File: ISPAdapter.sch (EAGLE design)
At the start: 3 parts

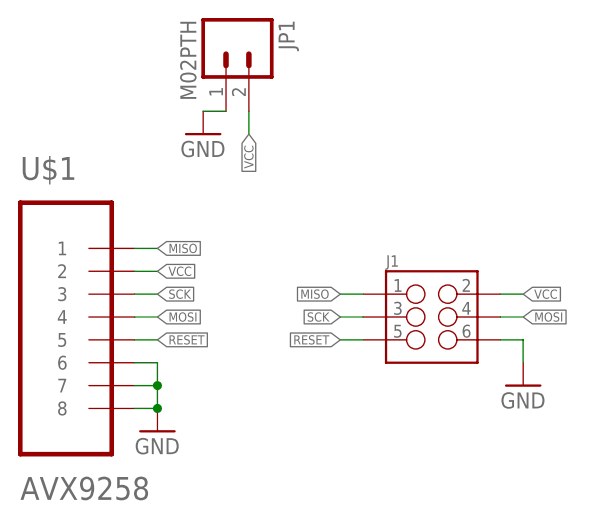
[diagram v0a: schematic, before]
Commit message: Dropped ground layer
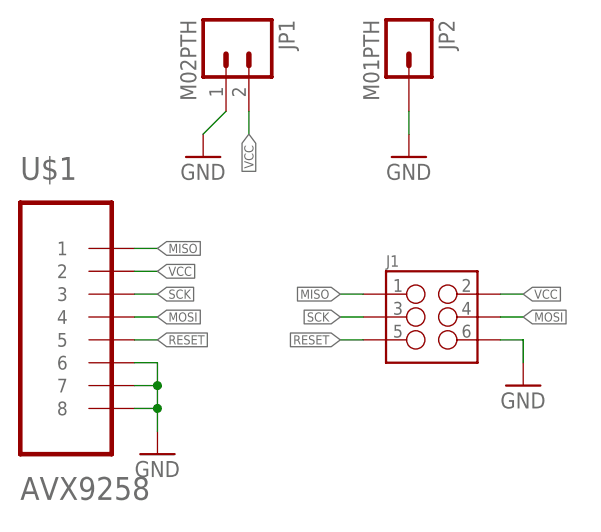
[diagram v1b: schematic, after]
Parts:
- added JP2: M01PTH, SparkFun-Connectors:M01PTH
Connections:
- net GND: now also JP2.1
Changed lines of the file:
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@@
 <part name="U$1" library="dubec" deviceset="AVX9258" device=""/>
 <part name="GND4" library="SparkFun-Aesthetics" deviceset="GND" device=""/>
+<part name="JP2" library="SparkFun-Connectors" deviceset="M01" device="PTH"/>
+<part name="GND1" library="SparkFun-Aesthetics" deviceset="GND" device=""/>
 </parts>
 <sheets>
@@
 <instance part="J1" gate="G$1" x="81.28" y="60.96"/>
 <instance part="JP1" gate="G$1" x="58.42" y="91.44" rot="R270"/>
-<instance part="GND3" gate="1" x="55.88" y="81.28"/>
+<instance part="GND3" gate="1" x="55.88" y="78.74"/>
 <instance part="U$1" gate="G$1" x="40.64" y="60.96"/>
-<instance part="GND4" gate="1" x="50.8" y="48.26"/>
+<instance part="GND4" gate="1" x="50.8" y="45.72"/>
+<instance part="JP2" gate="G$1" x="78.74" y="91.44" rot="R270"/>
+<instance part="GND1" gate="1" x="78.74" y="78.74"/>
 </instances>
 <busses>
@@
 <segment>
 <pinref part="JP1" gate="G$1" pin="1"/>
-<wire x1="58.42" y1="83.82" x2="55.88" y2="83.82" width="0.1524" layer="91"/>
+<wire x1="58.42" y1="83.82" x2="55.88" y2="81.28" width="0.1524" layer="91"/>
 <pinref part="GND3" gate="1" pin="GND"/>
 </segment>
 <segment>
 <pinref part="U$1" gate="G$1" pin="8"/>
-<wire x1="48.26" y1="50.8" x2="50.8" y2="50.8" width="0.1524" layer="91"/>
 <pinref part="GND4" gate="1" pin="GND"/>
 <pinref part="U$1" gate="G$1" pin="6"/>
@@
 <wire x1="50.8" y1="53.34" x2="50.8" y2="50.8" width="0.1524" layer="91"/>
 <junction x="50.8" y="53.34"/>
+<wire x1="50.8" y1="50.8" x2="50.8" y2="48.26" width="0.1524" layer="91"/>
+<wire x1="48.26" y1="50.8" x2="50.8" y2="50.8" width="0.1524" layer="91"/>
 <junction x="50.8" y="50.8"/>
 </segment>
+<segment>
+<pinref part="JP2" gate="G$1" pin="1"/>
+<pinref part="GND1" gate="1" pin="GND"/>
+<wire x1="78.74" y1="83.82" x2="78.74" y2="81.28" width="0.1524" layer="91"/>
+</segment>
 </net>

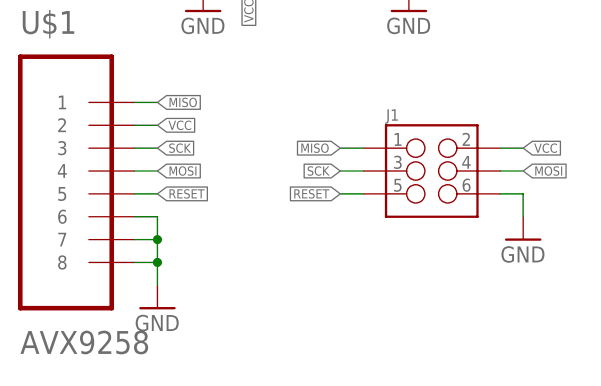
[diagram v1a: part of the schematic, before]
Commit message: Grounded screw holes; disconnected unused connector pins
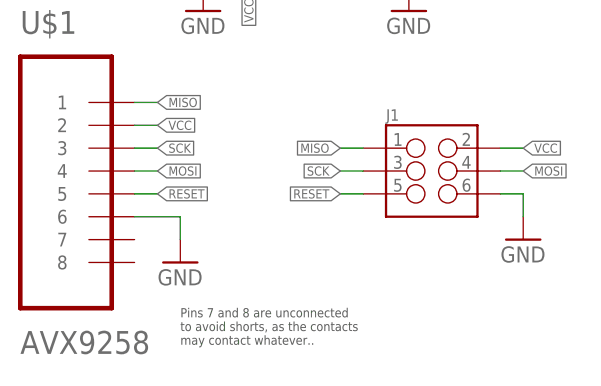
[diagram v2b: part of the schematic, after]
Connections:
- net GND: no longer U$1.7, U$1.8
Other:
- note added: "Pins 7 and 8 are unconnected to avoid shorts, as the contacts may contact whatever.."
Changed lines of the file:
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@@
 <sheet>
 <plain>
+<text x="53.34" y="45.72" size="1.016" layer="97" align="top-left">Pins 7 and 8 are unconnected
+to avoid shorts, as the contacts
+may contact whatever..</text>
 </plain>
 <instances>
@@
 <instance part="GND3" gate="1" x="55.88" y="78.74"/>
 <instance part="U$1" gate="G$1" x="40.64" y="60.96"/>
-<instance part="GND4" gate="1" x="50.8" y="45.72"/>
+<instance part="GND4" gate="1" x="53.34" y="50.8"/>
 <instance part="JP2" gate="G$1" x="78.74" y="91.44" rot="R270"/>
 <instance part="GND1" gate="1" x="78.74" y="78.74"/>
@@
 </segment>
 <segment>
-<pinref part="U$1" gate="G$1" pin="8"/>
-<pinref part="GND4" gate="1" pin="GND"/>
-<pinref part="U$1" gate="G$1" pin="6"/>
-<wire x1="48.26" y1="55.88" x2="50.8" y2="55.88" width="0.1524" layer="91"/>
-<pinref part="U$1" gate="G$1" pin="7"/>
-<wire x1="48.26" y1="53.34" x2="50.8" y2="53.34" width="0.1524" layer="91"/>
-<wire x1="50.8" y1="55.88" x2="50.8" y2="53.34" width="0.1524" layer="91"/>
-<wire x1="50.8" y1="53.34" x2="50.8" y2="50.8" width="0.1524" layer="91"/>
-<junction x="50.8" y="53.34"/>
-<wire x1="50.8" y1="50.8" x2="50.8" y2="48.26" width="0.1524" layer="91"/>
-<wire x1="48.26" y1="50.8" x2="50.8" y2="50.8" width="0.1524" layer="91"/>
-<junction x="50.8" y="50.8"/>
-</segment>
-<segment>
 <pinref part="JP2" gate="G$1" pin="1"/>
 <pinref part="GND1" gate="1" pin="GND"/>
 <wire x1="78.74" y1="83.82" x2="78.74" y2="81.28" width="0.1524" layer="91"/>
 </segment>
+<segment>
+<pinref part="U$1" gate="G$1" pin="6"/>
+<wire x1="48.26" y1="55.88" x2="53.34" y2="55.88" width="0.1524" layer="91"/>
+<pinref part="GND4" gate="1" pin="GND"/>
+<wire x1="53.34" y1="55.88" x2="53.34" y2="53.34" width="0.1524" layer="91"/>
+</segment>
 </net>

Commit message: Kelvin join?
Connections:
- new net DGND: J1.6, JP1.1, U$1.6
- net GND: no longer J1.6, JP1.1, U$1.6
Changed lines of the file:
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@@
 </segment>
 </net>
-<net name="GND" class="0">
+<net name="DGND" class="0">
 <segment>
 <pinref part="J1" gate="G$1" pin="6"/>
@@
 <wire x1="58.42" y1="83.82" x2="55.88" y2="81.28" width="0.1524" layer="91"/>
 <pinref part="GND3" gate="1" pin="GND"/>
-</segment>
-<segment>
-<pinref part="JP2" gate="G$1" pin="1"/>
-<pinref part="GND1" gate="1" pin="GND"/>
-<wire x1="78.74" y1="83.82" x2="78.74" y2="81.28" width="0.1524" layer="91"/>
 </segment>
 <segment>
@@
 </segment>
 </net>
+<net name="GND" class="0">
+<segment>
+<pinref part="JP2" gate="G$1" pin="1"/>
+<wire x1="78.74" y1="83.82" x2="78.74" y2="81.28" width="0.1524" layer="91"/>
+<pinref part="GND1" gate="1" pin="GND"/>
+</segment>
+</net>

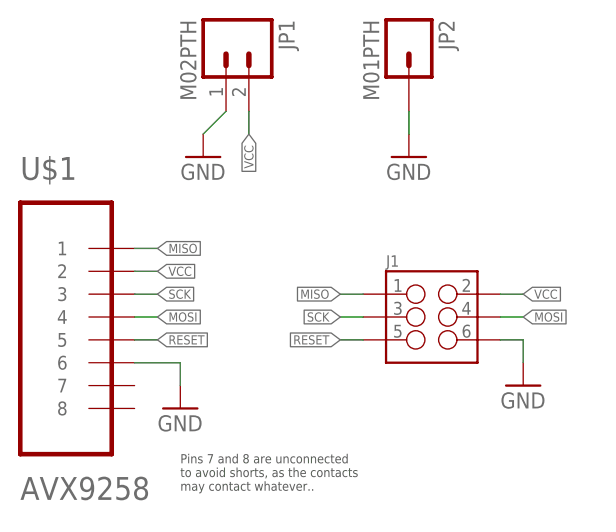
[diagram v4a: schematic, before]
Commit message: Adapter wiring to match DUBEC 1.5
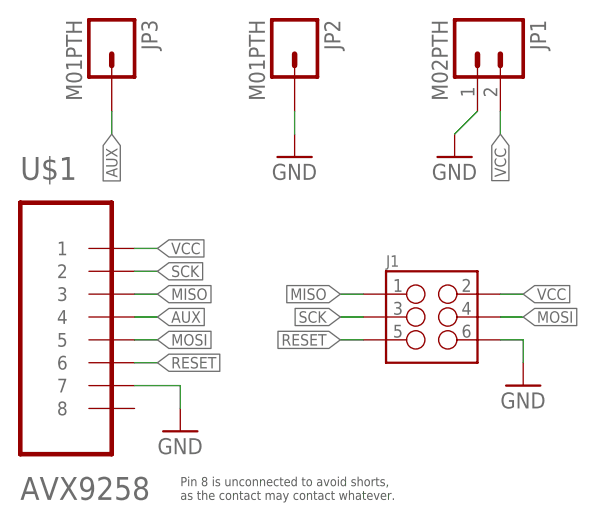
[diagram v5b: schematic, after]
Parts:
- added JP3: M01PTH, SparkFun-Connectors:M01PTH
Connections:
- new net AUX: JP3.1, U$1.4
- net DGND: now also U$1.7; no longer U$1.6
- net MISO: now also U$1.3; no longer U$1.1
- net MOSI: now also U$1.5; no longer U$1.4
- net RESET: now also U$1.6; no longer U$1.5
- net SCK: now also U$1.2; no longer U$1.3
- net VCC: now also U$1.1; no longer U$1.2
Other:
- note added: "Pin 8 is unconnected to avoid shorts, as the contact may contact whatever."
- note removed: "Pins 7 and 8 are unconnected to avoid shorts, as the contacts may contact whatever.."
- moved on the sheet: JP1, JP2
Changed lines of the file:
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@@
 <part name="JP2" library="SparkFun-Connectors" deviceset="M01" device="PTH"/>
 <part name="GND1" library="SparkFun-Aesthetics" deviceset="GND" device=""/>
+<part name="JP3" library="SparkFun-Connectors" deviceset="M01" device="PTH"/>
 </parts>
 <sheets>
 <sheet>
 <plain>
-<text x="53.34" y="45.72" size="1.016" layer="97" align="top-left">Pins 7 and 8 are unconnected
-to avoid shorts, as the contacts
-may contact whatever..</text>
+<text x="53.34" y="43.18" size="1.016" layer="97" align="top-left">Pin 8 is unconnected to avoid shorts,
+as the contact may contact whatever.</text>
 </plain>
 <instances>
 <instance part="GND2" gate="1" x="91.44" y="53.34"/>
 <instance part="J1" gate="G$1" x="81.28" y="60.96"/>
-<instance part="JP1" gate="G$1" x="58.42" y="91.44" rot="R270"/>
-<instance part="GND3" gate="1" x="55.88" y="78.74"/>
+<instance part="JP1" gate="G$1" x="86.36" y="91.44" rot="R270"/>
+<instance part="GND3" gate="1" x="83.82" y="78.74"/>
 <instance part="U$1" gate="G$1" x="40.64" y="60.96"/>
-<instance part="GND4" gate="1" x="53.34" y="50.8"/>
-<instance part="JP2" gate="G$1" x="78.74" y="91.44" rot="R270"/>
-<instance part="GND1" gate="1" x="78.74" y="78.74"/>
+<instance part="GND4" gate="1" x="53.34" y="48.26"/>
+<instance part="JP2" gate="G$1" x="66.04" y="91.44" rot="R270"/>
+<instance part="GND1" gate="1" x="66.04" y="78.74"/>
+<instance part="JP3" gate="G$1" x="45.72" y="91.44" rot="R270"/>
 </instances>
 <busses>
@@
 <pinref part="J1" gate="G$1" pin="2"/>
 <wire x1="88.9" y1="63.5" x2="91.44" y2="63.5" width="0.1524" layer="91"/>
-<label x="91.44" y="63.5" size="1.016" layer="95" xref="yes"/>
+<label x="91.44" y="63.5" size="1.27" layer="95" xref="yes"/>
 </segment>
 <segment>
 <pinref part="JP1" gate="G$1" pin="2"/>
-<wire x1="60.96" y1="83.82" x2="60.96" y2="81.28" width="0.1524" layer="91"/>
-<label x="60.96" y="81.28" size="1.016" layer="95" rot="R270" xref="yes"/>
+<wire x1="88.9" y1="83.82" x2="88.9" y2="81.28" width="0.1524" layer="91"/>
+<label x="88.9" y="81.28" size="1.27" layer="95" rot="R270" xref="yes"/>
 </segment>
 <segment>
-<pinref part="U$1" gate="G$1" pin="2"/>
-<wire x1="48.26" y1="66.04" x2="50.8" y2="66.04" width="0.1524" layer="91"/>
-<label x="50.8" y="66.04" size="1.016" layer="95" xref="yes"/>
+<pinref part="U$1" gate="G$1" pin="1"/>
+<wire x1="48.26" y1="68.58" x2="50.8" y2="68.58" width="0.1524" layer="91"/>
+<label x="50.8" y="68.58" size="1.27" layer="95" xref="yes"/>
 </segment>
 </net>
@@
 <pinref part="J1" gate="G$1" pin="4"/>
 <wire x1="88.9" y1="60.96" x2="91.44" y2="60.96" width="0.1524" layer="91"/>
-<label x="91.44" y="60.96" size="1.016" layer="95" xref="yes"/>
+<label x="91.44" y="60.96" size="1.27" layer="95" xref="yes"/>
 </segment>
 <segment>
-<pinref part="U$1" gate="G$1" pin="4"/>
-<wire x1="48.26" y1="60.96" x2="50.8" y2="60.96" width="0.1524" layer="91"/>
-<label x="50.8" y="60.96" size="1.016" layer="95" xref="yes"/>
+<pinref part="U$1" gate="G$1" pin="5"/>
+<wire x1="48.26" y1="58.42" x2="50.8" y2="58.42" width="0.1524" layer="91"/>
+<label x="50.8" y="58.42" size="1.27" layer="95" xref="yes"/>
 </segment>
 </net>
@@
 <segment>
 <pinref part="JP1" gate="G$1" pin="1"/>
-<wire x1="58.42" y1="83.82" x2="55.88" y2="81.28" width="0.1524" layer="91"/>
+<wire x1="86.36" y1="83.82" x2="83.82" y2="81.28" width="0.1524" layer="91"/>
 <pinref part="GND3" gate="1" pin="GND"/>
 </segment>
 <segment>
-<pinref part="U$1" gate="G$1" pin="6"/>
-<wire x1="48.26" y1="55.88" x2="53.34" y2="55.88" width="0.1524" layer="91"/>
 <pinref part="GND4" gate="1" pin="GND"/>
-<wire x1="53.34" y1="55.88" x2="53.34" y2="53.34" width="0.1524" layer="91"/>
+<wire x1="53.34" y1="53.34" x2="53.34" y2="50.8" width="0.1524" layer="91"/>
+<pinref part="U$1" gate="G$1" pin="7"/>
+<wire x1="53.34" y1="53.34" x2="48.26" y2="53.34" width="0.1524" layer="91"/>
 </segment>
 </net>
@@
 <pinref part="J1" gate="G$1" pin="1"/>
 <wire x1="73.66" y1="63.5" x2="71.12" y2="63.5" width="0.1524" layer="91"/>
-<label x="71.12" y="63.5" size="1.016" layer="95" rot="R180" xref="yes"/>
+<label x="71.12" y="63.5" size="1.27" layer="95" rot="R180" xref="yes"/>
 </segment>
 <segment>
-<pinref part="U$1" gate="G$1" pin="1"/>
-<wire x1="48.26" y1="68.58" x2="50.8" y2="68.58" width="0.1524" layer="91"/>
-<label x="50.8" y="68.58" size="1.016" layer="95" xref="yes"/>
+<pinref part="U$1" gate="G$1" pin="3"/>
+<wire x1="48.26" y1="63.5" x2="50.8" y2="63.5" width="0.1524" layer="91"/>
+<label x="50.8" y="63.5" size="1.27" layer="95" xref="yes"/>
 </segment>
 </net>
@@
 <pinref part="J1" gate="G$1" pin="3"/>
 <wire x1="73.66" y1="60.96" x2="71.12" y2="60.96" width="0.1524" layer="91"/>
-<label x="71.12" y="60.96" size="1.016" layer="95" rot="R180" xref="yes"/>
+<label x="71.12" y="60.96" size="1.27" layer="95" rot="R180" xref="yes"/>
 </segment>
 <segment>
-<pinref part="U$1" gate="G$1" pin="3"/>
-<wire x1="48.26" y1="63.5" x2="50.8" y2="63.5" width="0.1524" layer="91"/>
-<label x="50.8" y="63.5" size="1.016" layer="95" xref="yes"/>
+<pinref part="U$1" gate="G$1" pin="2"/>
+<wire x1="48.26" y1="66.04" x2="50.8" y2="66.04" width="0.1524" layer="91"/>
+<label x="50.8" y="66.04" size="1.27" layer="95" xref="yes"/>
 </segment>
 </net>
@@
 <pinref part="J1" gate="G$1" pin="5"/>
 <wire x1="73.66" y1="58.42" x2="71.12" y2="58.42" width="0.1524" layer="91"/>
-<label x="71.12" y="58.42" size="1.016" layer="95" rot="R180" xref="yes"/>
+<label x="71.12" y="58.42" size="1.27" layer="95" rot="R180" xref="yes"/>
 </segment>
 <segment>
-<pinref part="U$1" gate="G$1" pin="5"/>
-<wire x1="48.26" y1="58.42" x2="50.8" y2="58.42" width="0.1524" layer="91"/>
-<label x="50.8" y="58.42" size="1.016" layer="95" xref="yes"/>
+<pinref part="U$1" gate="G$1" pin="6"/>
+<wire x1="48.26" y1="55.88" x2="50.8" y2="55.88" width="0.1524" layer="91"/>
+<label x="50.8" y="55.88" size="1.27" layer="95" xref="yes"/>
 </segment>
 </net>
@@
 <segment>
 <pinref part="JP2" gate="G$1" pin="1"/>
-<wire x1="78.74" y1="83.82" x2="78.74" y2="81.28" width="0.1524" layer="91"/>
+<wire x1="66.04" y1="83.82" x2="66.04" y2="81.28" width="0.1524" layer="91"/>
 <pinref part="GND1" gate="1" pin="GND"/>
 </segment>
 </net>
+<net name="AUX" class="0">
+<segment>
+<pinref part="U$1" gate="G$1" pin="4"/>
+<wire x1="48.26" y1="60.96" x2="50.8" y2="60.96" width="0.1524" layer="91"/>
+<label x="50.8" y="60.96" size="1.27" layer="95" xref="yes"/>
+</segment>
+<segment>
+<pinref part="JP3" gate="G$1" pin="1"/>
+<wire x1="45.72" y1="83.82" x2="45.72" y2="81.28" width="0.1524" layer="91"/>
+<label x="45.72" y="81.28" size="1.27" layer="95" rot="R270" xref="yes"/>
+</segment>
+</net>

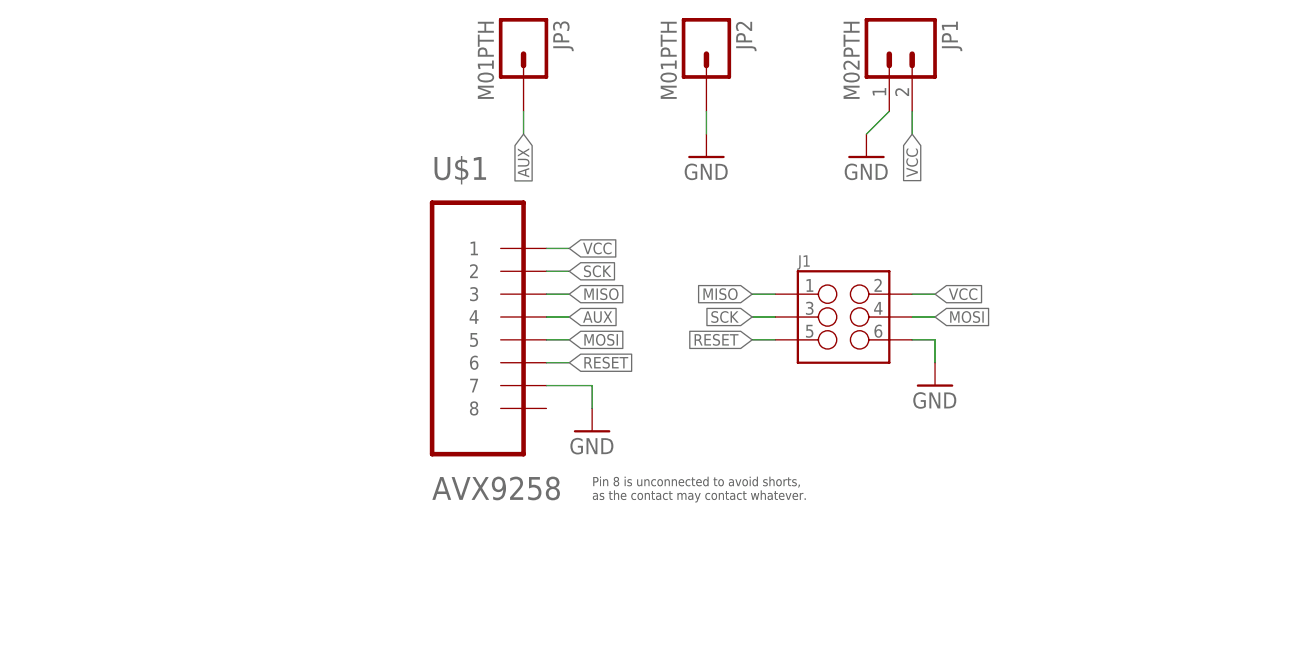
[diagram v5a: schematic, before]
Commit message: ISP/DW-switch
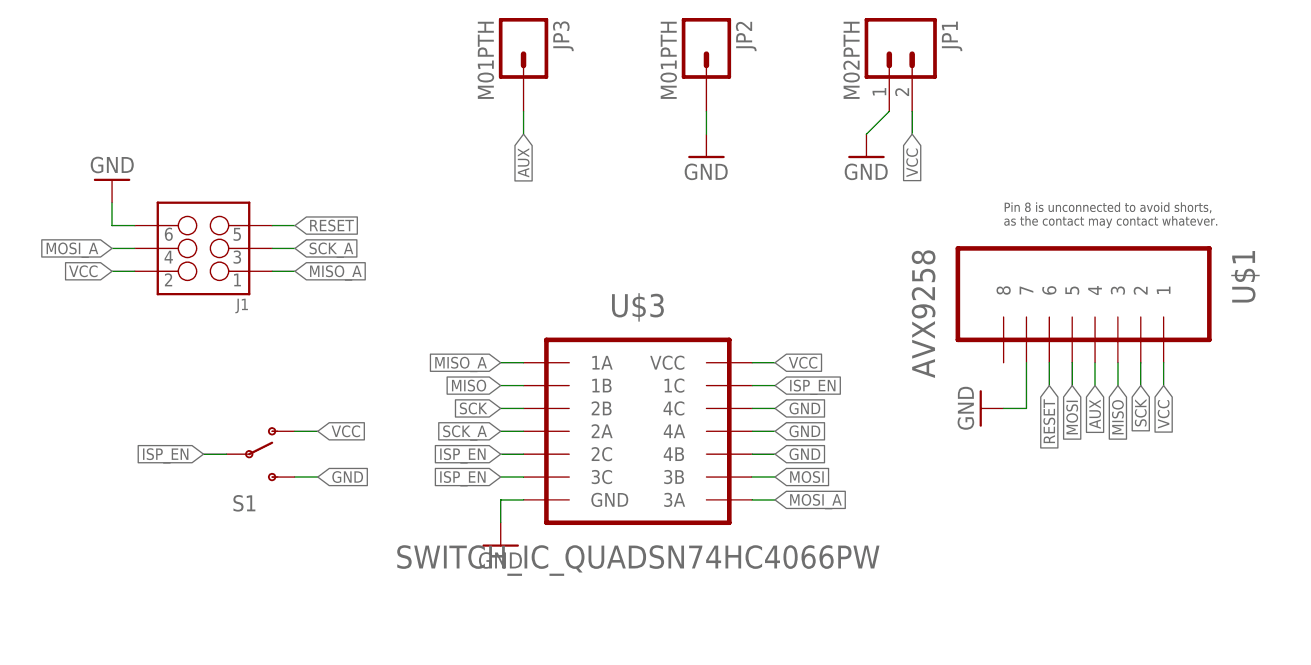
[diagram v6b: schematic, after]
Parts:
- added S1: (no value), SparkFun-Electromechanical:SWITCH-SPDTESWITCH
- added U$3: SWITCH_IC_QUADSN74HC4066PW, dubec:SWITCH_IC_QUADSN74HC4066PW
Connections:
- new net ISP_EN: S1.P, U$3.1C, U$3.2C, U$3.3C
- new net MISO_A: J1.1, U$3.1A
- new net MOSI_A: J1.4, U$3.3A
- new net SCK_A: J1.3, U$3.2A
- net GND: now also S1.S, U$3.4A, U$3.4B, U$3.4C, U$3.GND
- net MISO: now also U$3.1B; no longer J1.1
- net MOSI: now also U$3.3B; no longer J1.4
- net SCK: now also U$3.2B; no longer J1.3
- net VCC: now also S1.O, U$3.VCC
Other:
- moved on the sheet: J1, U$1
